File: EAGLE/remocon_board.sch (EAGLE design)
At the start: 56 parts, among them CN1 POWER_IF, CN2 PICkit_IF, CN3 ROTARY_ENCODER, Q1 2SC1815, Q2 2N7000, SW1 10-XX, SW2 10-XX, SW3 10-XX, SW4 10-XX, SW5 10-XX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

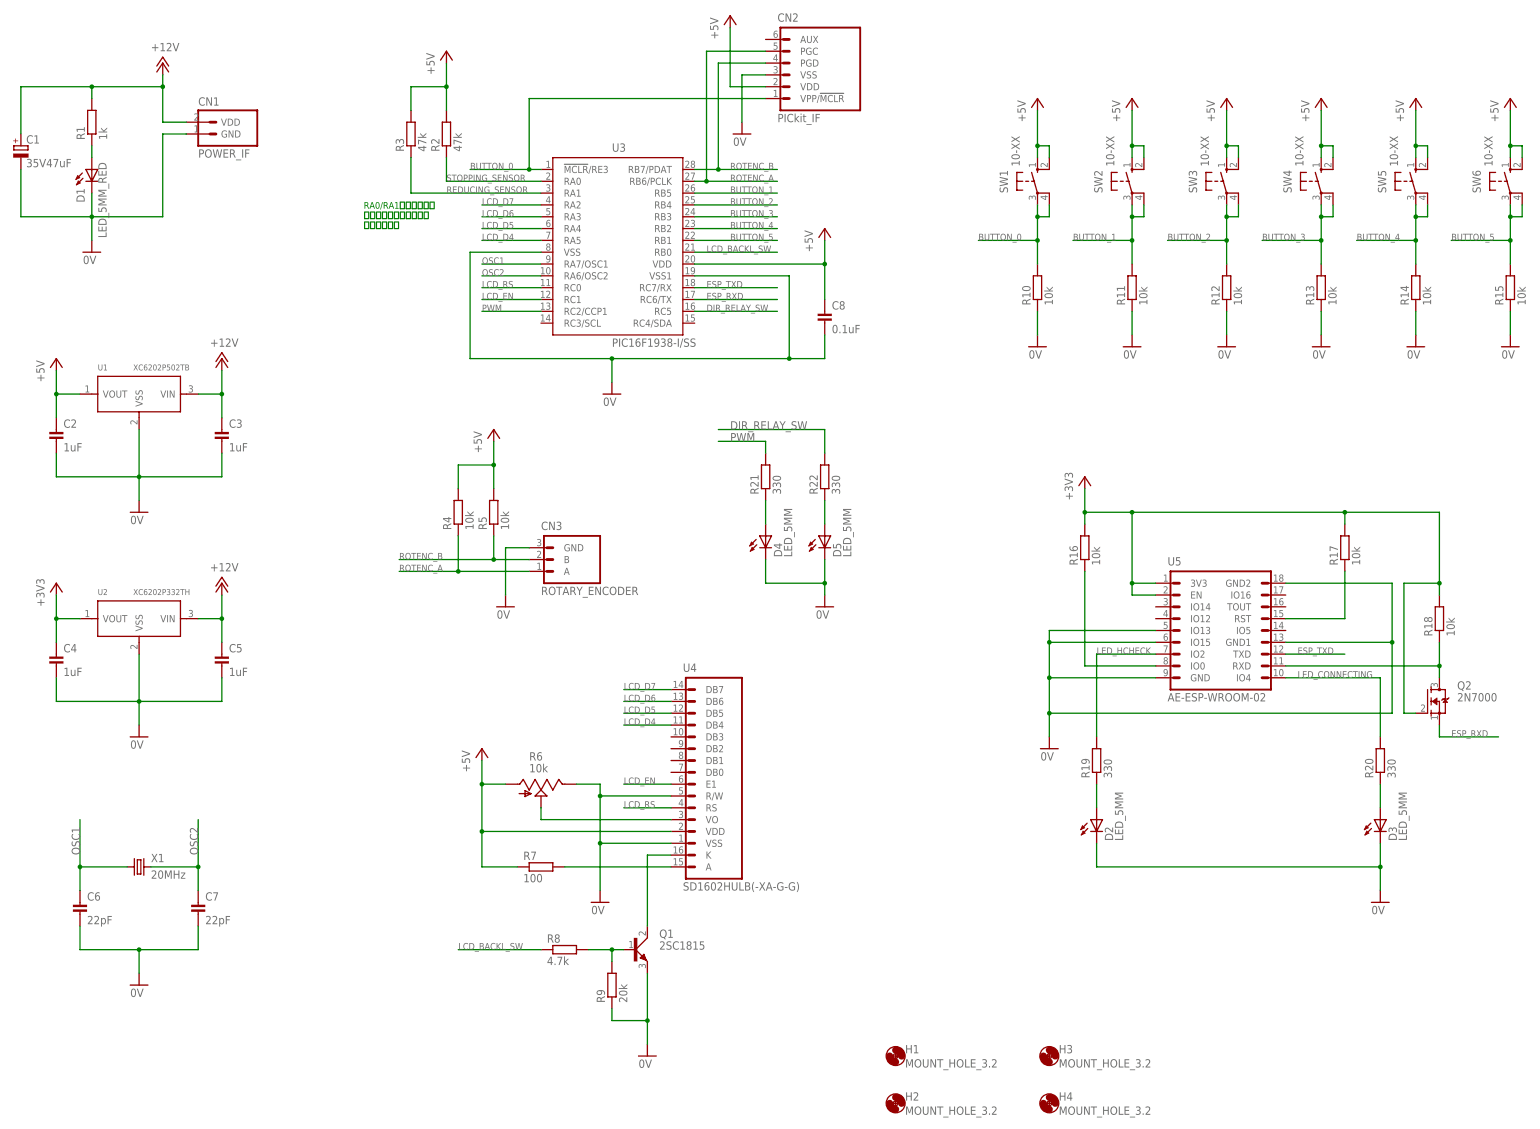
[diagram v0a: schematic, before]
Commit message: Wi-Fi部が不要になったため回路図から削除
別途作成のWi-Fi HTTP通信基板に接続する前提
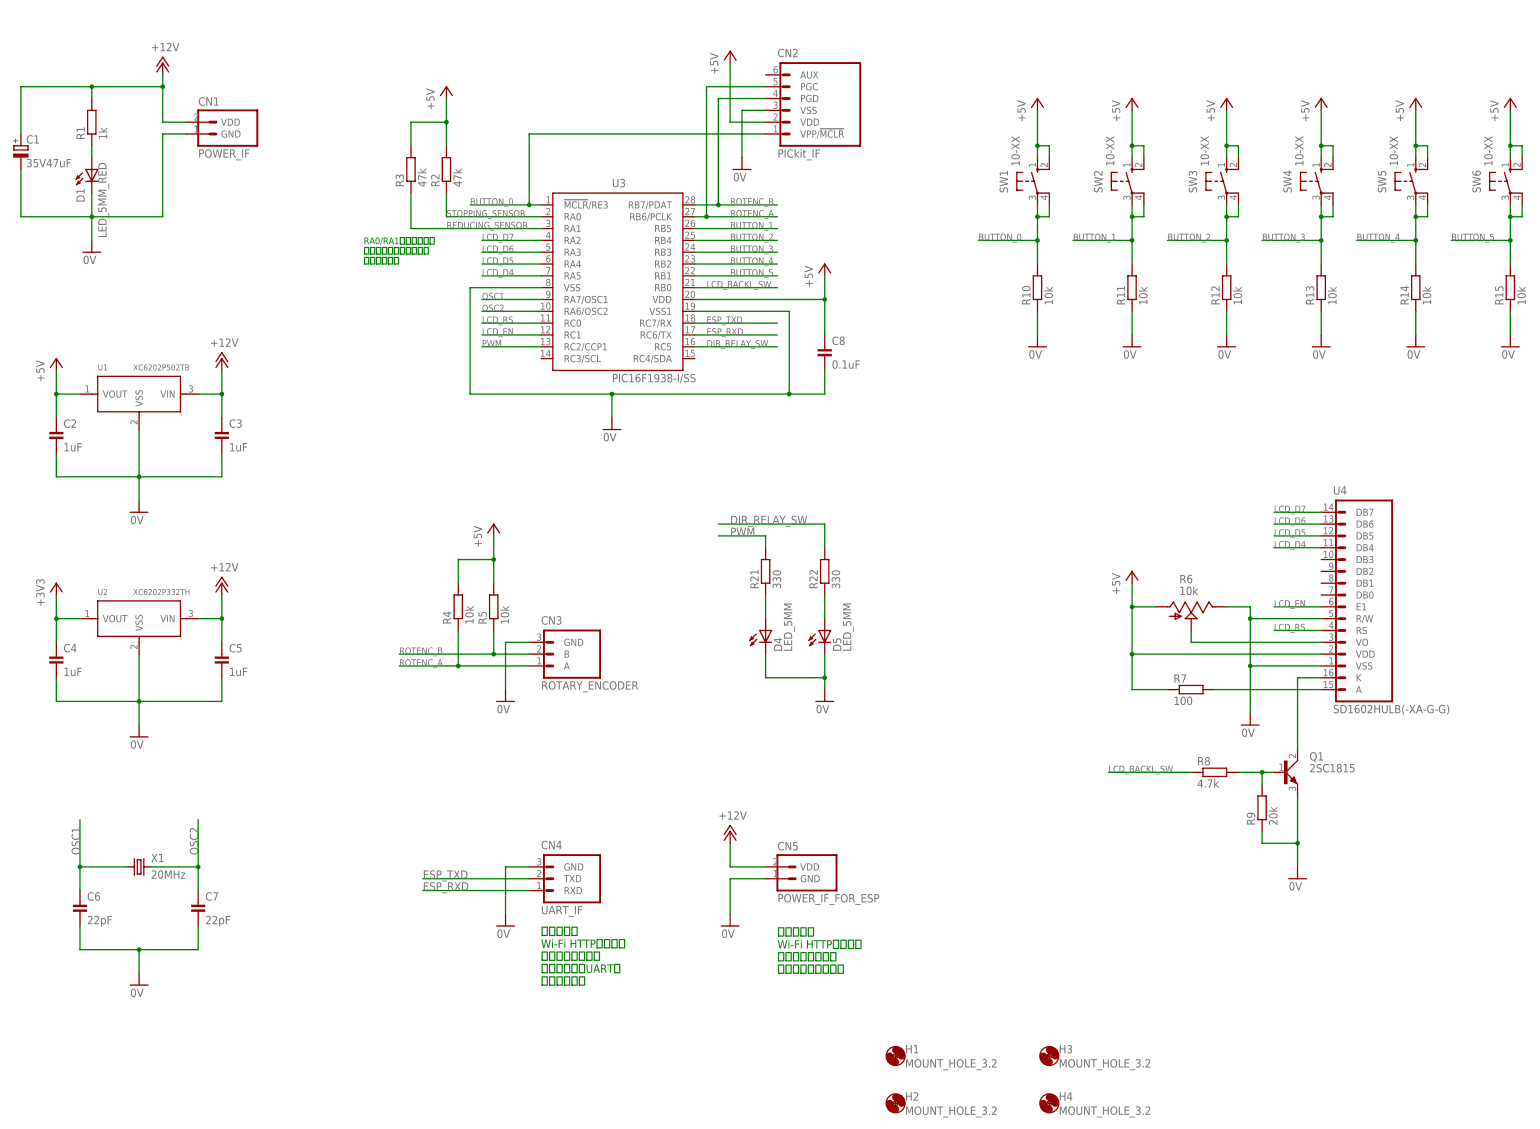
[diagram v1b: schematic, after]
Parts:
- removed D2, D3: LED_5MM, Parts:LED_5MM
- removed Q2: 2N7000, Parts:2N7000
- removed R16, R17, R18: 10k, Parts:RESISTOR_300MIL
- removed R19, R20: 330, Parts:RESISTOR_300MIL
- removed U5: AE-ESP-WROOM-02, PartsForProto:AE-ESP-WROOM-02
- added CN4: UART_IF, PartsForProto:UART_IF
- added CN5: POWER_IF_FOR_ESP, PartsForProto:POWER_IF
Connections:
- removed net +3V3: Q2.G, R16.2, R17.2, R18.2, U5.3V3, U5.EN
- removed net LED_CONNECTING: R20.2, U5.IO4
- removed net LED_HCHECK: R19.2, U5.IO2
- removed net N$10: R17.1, U5.RST
- removed net N$11: D3.A, R20.1
- removed net N$12: D2.A, R19.1
- removed net N$7: Q2.D, R18.1, U5.RXD
- removed net N$9: R16.1, U5.IO0
- net +12V: now also CN5.VDD
- net 0V: now also CN4.GND, CN5.GND; no longer D2.C, D3.C, U5.GND, U5.GND1, U5.GND2, U5.IO13, U5.IO15
- net ESP_RXD: now also CN4.RXD; no longer Q2.S
- net ESP_TXD: now also CN4.TXD; no longer U5.TXD
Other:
- note added: "別途作成の Wi-Fi HTTP通信基板 （子機モード）の ソフトウェアUARTに 接続します。"
- note added: "別途作成の Wi-Fi HTTP通信基板 （子機モード）へ 電源を供給します。"
- moved on the sheet: C8, CN2, CN3, D4, D5, Q1, R2, R21, R22, R3, R4, R5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
